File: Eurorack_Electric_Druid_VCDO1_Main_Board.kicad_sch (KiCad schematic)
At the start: 0 parts

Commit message: Multiboard work update
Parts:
- added C10, C11, C13, C14, C15, C9: 330pF, DIYSynthMNL:C_Rect_L7.0mm_W2.0mm_P5.00mm_BigPads, symbol Device:C
- added C12, C16: 150pF, DIYSynthMNL:C_Rect_L7.0mm_W2.0mm_P5.00mm_BigPads, symbol Device:C
- added C17, C18, C19, C24: 0.1uF, DIYSynthMNL:C_Rect_L7.0mm_W2.0mm_P5.00mm_BigPads, symbol Device:C
- added C19, C24: 22uF, DIYSynthMNL:CP_Radial_D4.0mm_P1.50mm, symbol Device:C_Polarized
- added C3, C4, C6, C7: 2.2uF, DIYSynthMNL:CP_Radial_D5.0mm_P2.50mm, symbol Device:C_Polarized
- added C5, C8: 100nF, DIYSynthMNL:C_Rect_L7.0mm_W2.0mm_P5.00mm_BigPads, symbol Device:C
- added D10, D11, D12, D13, D14, D15, D16, D3, D4, D5, D6, D7, D8, D9: BAT42, Diode_THT:D_DO-35_SOD27_P7.62mm_Horizontal, symbol Diode:BAT42
- added D13, D14: 4001, DIYSynthMNL:D_DO-41_SOD81_P7.62mm_Horizontal_BigPads, symbol Device:D
- added H3, H4: MountingHole_Pad, DIYSynthMNL:MountingHole_M3_Standoff_Pad, symbol Mechanical:MountingHole_Pad
- added J1: EuroPower_JST_3P, DIYSynthMNL:Eurorack_power_jst_3P, symbol DIYSynthMNL:JST_Eurorack_power_3P
- added J2: EURO_PWR_16P, DIYSynthMNL:IDC-Header_2x08_P2.54mm_Vertical, symbol DIYSynthMNL:EURO_PWR_16_PIN
- added Q1: 2N3904, Package_TO_SOT_THT:TO-92_Inline, symbol Transistor_BJT:2N3904
- added R1, R2: *10k, DIYSynthMNL:R_quarter_watt_L6.3mm_D2.5mm_P7.62mm, symbol Device:R
- added R10, R15, R18, R20, R25, R29, R33, R37, R47, R51, R9: 100K, DIYSynthMNL:R_quarter_watt_L6.3mm_D2.5mm_P7.62mm, symbol Device:R
- added R11, R19: 1K, DIYSynthMNL:R_quarter_watt_L6.3mm_D2.5mm_P7.62mm, symbol Device:R
- added R12, R16, R4, R5: 20K, DIYSynthMNL:R_quarter_watt_L6.3mm_D2.5mm_P7.62mm, symbol Device:R
- added R13, R17, R6, R7: 27K, DIYSynthMNL:R_quarter_watt_L6.3mm_D2.5mm_P7.62mm, symbol Device:R
- added R14, R8: 51K, DIYSynthMNL:R_quarter_watt_L6.3mm_D2.5mm_P7.62mm, symbol Device:R
- added R21: 1M, DIYSynthMNL:R_quarter_watt_L6.3mm_D2.5mm_P7.62mm, symbol Device:R
- added R22: 10K, DIYSynthMNL:R_quarter_watt_L6.3mm_D2.5mm_P7.62mm, symbol Device:R
- added R24, R27: 91K, DIYSynthMNL:R_quarter_watt_L6.3mm_D2.5mm_P7.62mm, symbol Device:R
- added R26, R31, R34, R38, R48, R52: 4K7, DIYSynthMNL:R_quarter_watt_L6.3mm_D2.5mm_P7.62mm, symbol Device:R
- added R28, R32, R35, R36, R39, R46, R49, R50, R53: 200K, DIYSynthMNL:R_quarter_watt_L6.3mm_D2.5mm_P7.62mm, symbol Device:R
- added R3: 10k, DIYSynthMNL:R_quarter_watt_L6.3mm_D2.5mm_P7.62mm, symbol Device:R
- added R30: 180K, DIYSynthMNL:R_quarter_watt_L6.3mm_D2.5mm_P7.62mm, symbol Device:R
- added RV1: 20K_V/Oct_Adjust, DIYSynthMNL:Potentiometer_Bourns_3296W_Vertical_BigPads, symbol Device:R_Potentiometer_Trim
- added RV2: 20K_Offset_trim, DIYSynthMNL:Potentiometer_Bourns_3296W_Vertical_BigPads, symbol Device:R_Potentiometer_Trim
- added RV4: 47K_Zero_Trim, DIYSynthMNL:Potentiometer_Bourns_3296W_Vertical_BigPads, symbol Device:R_Potentiometer_Trim
- added U1: 78M05, Package_TO_SOT_SMD:TO-252-2, symbol Regulator_Linear:LM78M05_TO252
- added U2: 79M05, Package_TO_SOT_SMD:TO-252-2, symbol Regulator_Linear:MC79M05_TO252
- added U3: VCDO1, DIYSynthMNL:DIP-18_W7.62mm_LongPads, symbol DIYSynthMNL:Druid_VCDO1_PIC16F1847
- added U4, U6: TL074, DIYSynthMNL:DIP-14_W7.62mm_LongPads, symbol Amplifier_Operational:TL074
- added U5, U7: TL072, DIYSynthMNL:DIP-8_W7.62mm_LongPads, symbol Amplifier_Operational:TL072
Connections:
- new net: R50.2, R51.1, R53.2, U7.6 (-)
- new net: R25.1, R27.2, RV1.2, RV1.3, U6.2 (-)
- new net: R25.2, R26.1, U6.1
- new net: R30.1, RV4.2, RV4.3
- new net: R28.2, R29.1, R30.2, U6.6 (-)
- new net: R29.2, R31.1, U6.7
- new net: C9.1, R4.2, R5.1
- new net: R14.2, R15.1, R18.2, U5.6 (-)
- new net: R15.2, R19.1, U5.7
- new net: R27.1, RV2.2, RV2.3
- new net: C16.2, R17.1, U4.12 (+)
- new net: R32.2, R33.1, R35.2, U6.9 (-)
- new net: R33.2, R34.1, U6.8
- new net: C14.2, R14.1, U4.13 (-), U4.14
- new net: R10.1, R8.2, R9.2, U5.2 (-)
- new net: R10.2, R11.1, U5.1
- new net: R51.2, R52.1, U7.7
- new net: C11.2, R5.2, U4.3 (+)
- new net: D3.2 (A), D4.1 (K), Q1.2 (B), R20.2, R21.1
- new net: C14.1, R13.2, R17.2
- new net: C10.2, R8.1, U4.6 (-), U4.7
- new net: R24.2, RV1.1
- new net: C13.1, R12.2, R16.1
- new net: R37.2, R38.1, U6.14
- new net: R3.2, U3.15 (Unused)
- new net: R36.2, R37.1, R39.2, U6.13 (-)
- new net: C9.2, R6.1, U4.1, U4.2 (-)
- new net: C13.2, R13.1, U4.8, U4.9 (-)
- new net: R46.2, R47.1, R49.2, U7.2 (-)
- new net: C15.2, R16.2, U4.10 (+)
- new net: C12.2, R7.1, U4.5 (+)
- new net: R47.2, R48.1, U7.1
- new net: C10.1, R6.2, R7.2
- new net +12V: C17.1, C18.1, C19.1, C19.1, C24.1, C3.1, D13.1 (K), U1.1 (VI), U4.4 (V+), U5.8 (V+), U6.4 (V+), U7.8 (V+)
- new net +12V_IN: D13.2 (A), J1.1 (+12v), J2.10 (+12V), J2.9 (+12V)
- new net +5V: C4.1, C5.1, D11.1 (K), D13.1 (K), D15.1 (K), D3.1 (K), D5.1 (K), D7.1 (K), D9.1 (K), R1.1, R22.1, R3.1, U1.3 (VO), U3.14 (+5V)
- new net -12V: C17.2, C18.2, C19.2, C24.2, C24.2, C6.2, D14.2 (A), U2.2 (VI), U4.11 (V-), U5.4 (V-), U6.11 (V-), U7.4 (V-)
- new net -12V_IN: D14.1 (K), J1.3 (-12v), J2.1 (-12V), J2.2 (-12V)
- new net -5V: C7.2, C8.2, R18.1, R2.2, R35.1, R39.1, R49.1, R53.1, R9.1, RV2.1, RV4.1, U2.3 (VO)
- new net AIN_Bitcrush_Control: D15.2 (A), D16.1 (K), R52.2, U3.9 (Bitcrush_Control)
- new net AIN_Freq_Mod_CV: D7.2 (A), D8.1 (K), R31.2, U3.11 (Freq_Mod_CV)
- new net AIN_Glide_Control: D13.2 (A), D14.1 (K), R48.2, U3.8 (Glide_Control)
- new net AIN_Note_CV: D5.2 (A), D6.1 (K), R26.2, U3.10 (Note_CV)
- new net AIN_Sub_Select_CV: D11.2 (A), D12.1 (K), R38.2, U3.18 (Sub_Select_CV)
- new net AIN_Waveform_CV: D10.1 (K), D9.2 (A), R34.2, U3.17 (Waveform_CV)
- new net Bitcrush_CV: R50.1
- new net DIN_Glide_Input: Q1.3 (C), R22.2, U3.13 (Glide_Input)
- new net DOUT_Main_Osc_Out: R4.1, U3.6 (Main_Osc_Out)
- new net DOUT_Sub_OSC_Out: R12.1, U3.16 (Sub_OSC_out)
- new net FM_CV: R28.1
- new net Freq_Course_Ctrl: U3.1 (Freq_Control)
- new net Freq_Fine_Ctrl: U3.2 (Fine_Control)
- new net GND: C11.1, C12.1, C15.1, C16.1, C19.2, C24.1, C3.2, C4.2, C5.2, C6.1, C7.1, C8.1, D10.2 (A), D12.2 (A), D14.2 (A), D16.2 (A), D4.2 (A), D6.2 (A), D8.2 (A), H3.1, H4.1, J1.2 (GND), J2.3 (GND), J2.4 (GND), J2.5 (GND), J2.6 (GND), J2.7 (GND), J2.8 (GND), Q1.1 (E), R1.2, R2.1, R21.2, U1.2 (GND), U2.1 (GND), U3.5 (0v), U5.3 (+), U5.5 (+), U6.10 (+), U6.12 (+), U6.3 (+), U6.5 (+), U7.3 (+), U7.5 (+)
- new net GlideTime_CV: R46.1
- new net Glide_OnOff_CV: R20.1
- new net MainOsc_Out: R11.2
- new net MainWaveSel_CV: R32.1
- new net MainWaveSel_Ctrl: U3.3 (Waveform_Control)
- new net Note_CV: R24.1
- new net SubOsc_Out: R19.2
- new net SubWaveSel_CV: R36.1
- new net SubWaveSel_Ctrl: U3.7 (Sub_Select_Control)
- no-connect marks 0 -> 8
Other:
- note added: "*Optional Load Resistor"
- note added: "0V-5V"
- note added: "18KHz Bessel Filter 24dB/Oct"
- note added: "Bitcrush CV"
- note added: "CV=Jacks Control=Pots"
- note added: "FM CV"
- note added: "Glide CV"
- note added: "Glide on/off CV"
- note added: "Main Wave Select CV"
- note added: "Main oscillator"
- note added: "Note CV"
- note added: "Output processing"
- note added: "Power"
- note added: "Sub Wave Select CV"
- note added: "Sub oscillator"
- note added: "The Druid datasheet has a design error with the negative 5 volt regulator."

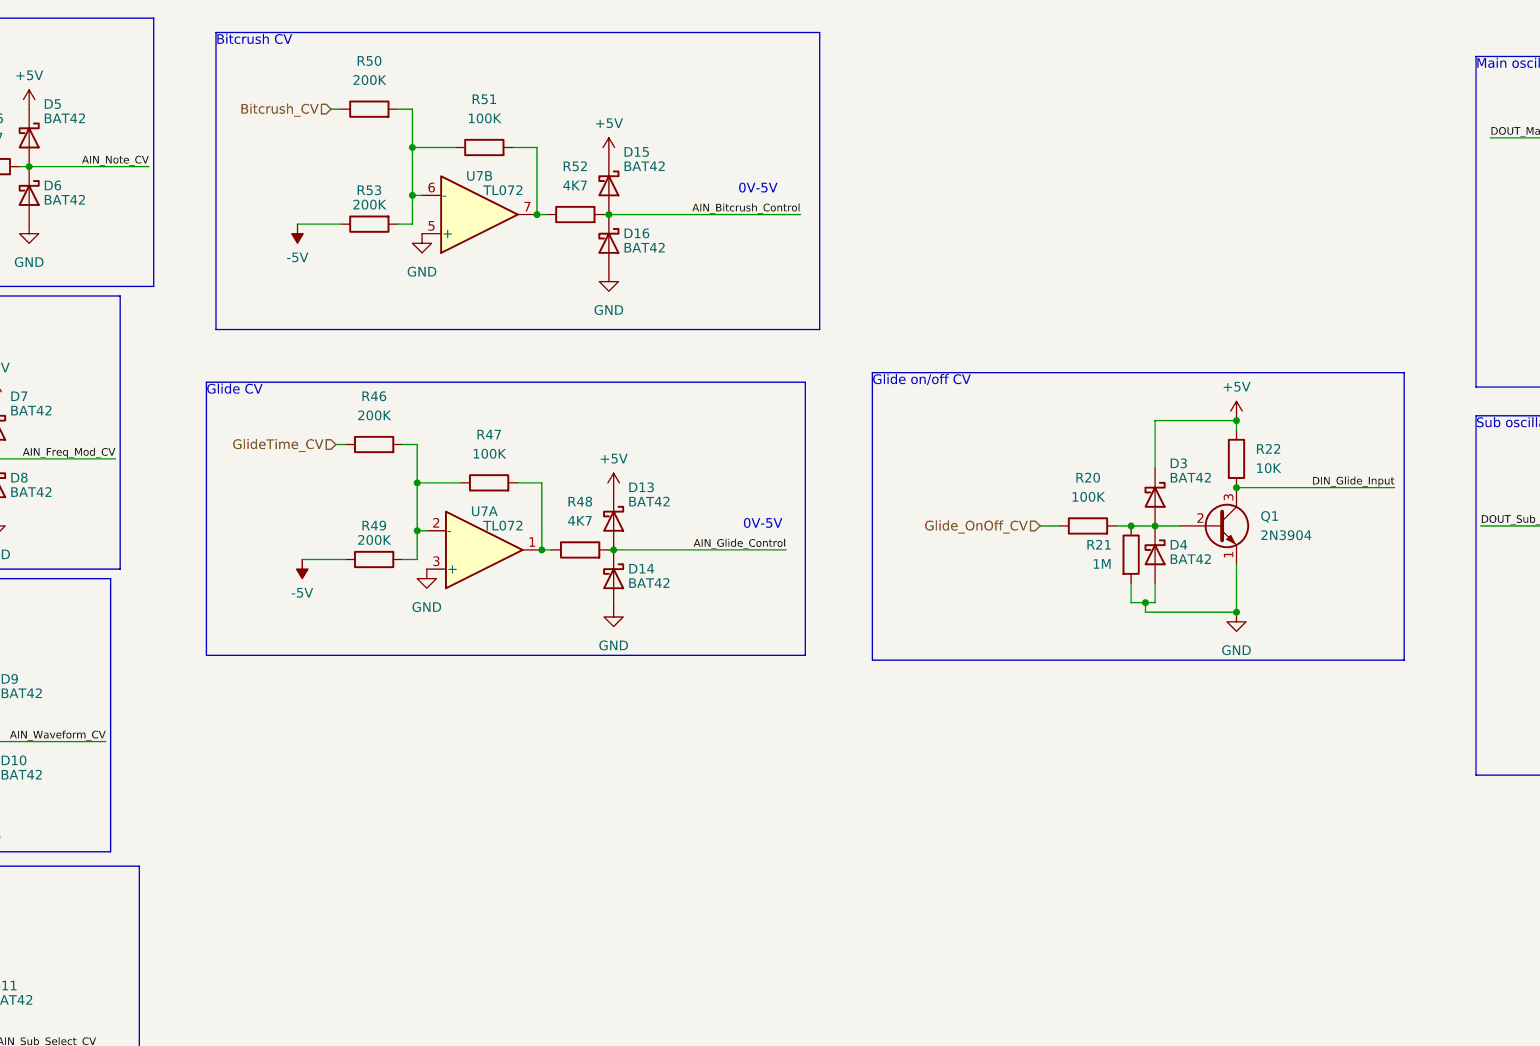
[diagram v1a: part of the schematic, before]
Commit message: updated schematic to rev 0.1.1
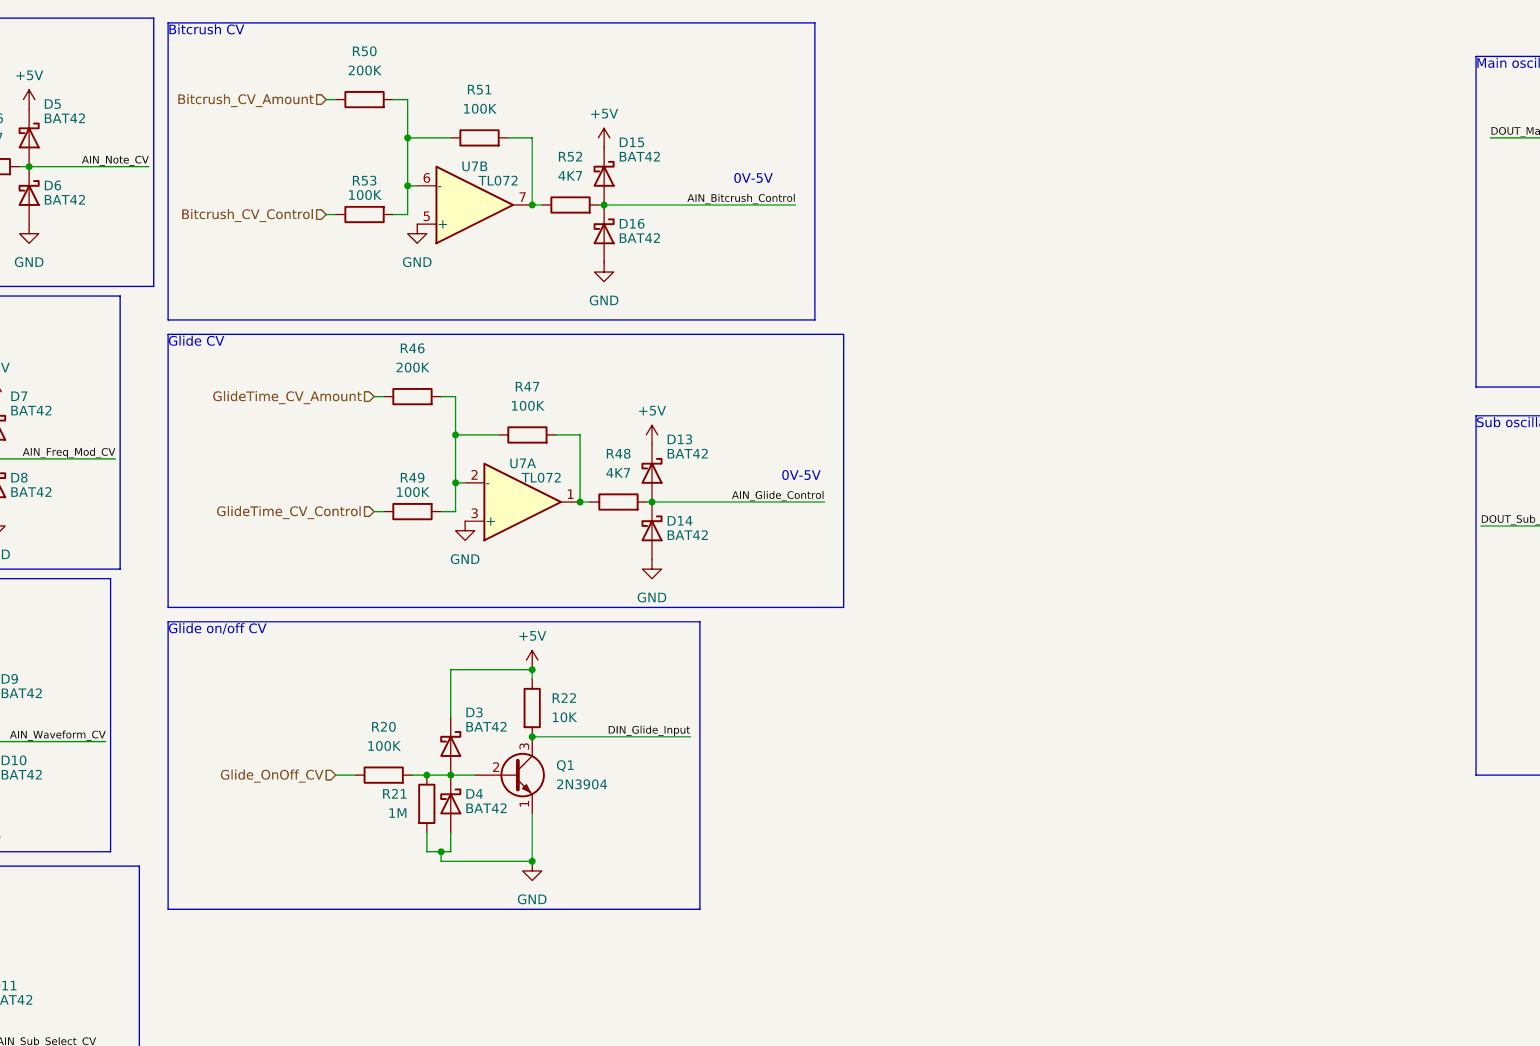
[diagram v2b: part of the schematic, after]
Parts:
- R49, R53: value 200K -> 100K
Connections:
- net -5V: no longer R49.1, R53.1
- net Bitcrush_CV renamed Bitcrush_CV_Amount
- net GlideTime_CV renamed GlideTime_CV_Amount
- new net Bitcrush_CV_Control: R53.1
- new net GlideTime_CV_Control: R49.1
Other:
- moved on the sheet: D13, D14, D15, D16, D3, D4, Q1, R20, R21, R22, R46, R47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

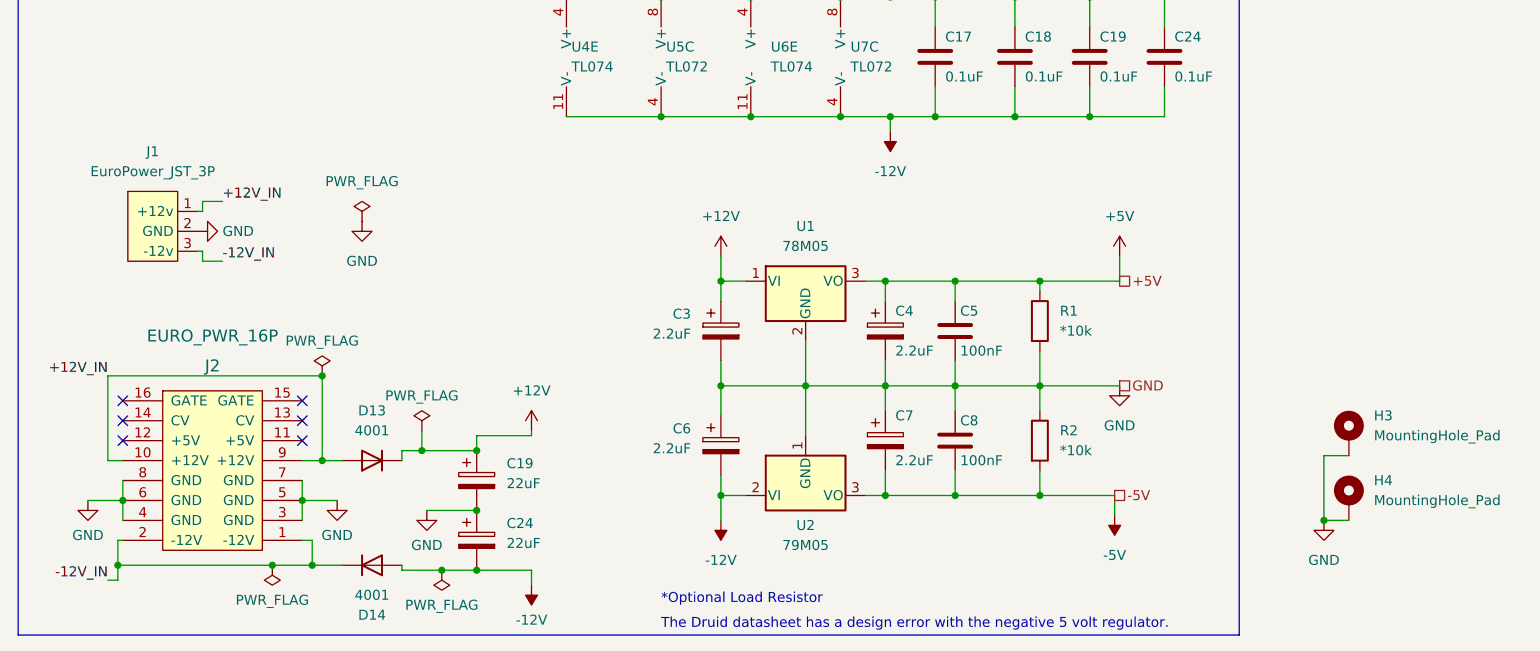
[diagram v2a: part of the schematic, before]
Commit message: updated to schematic revision 1.2
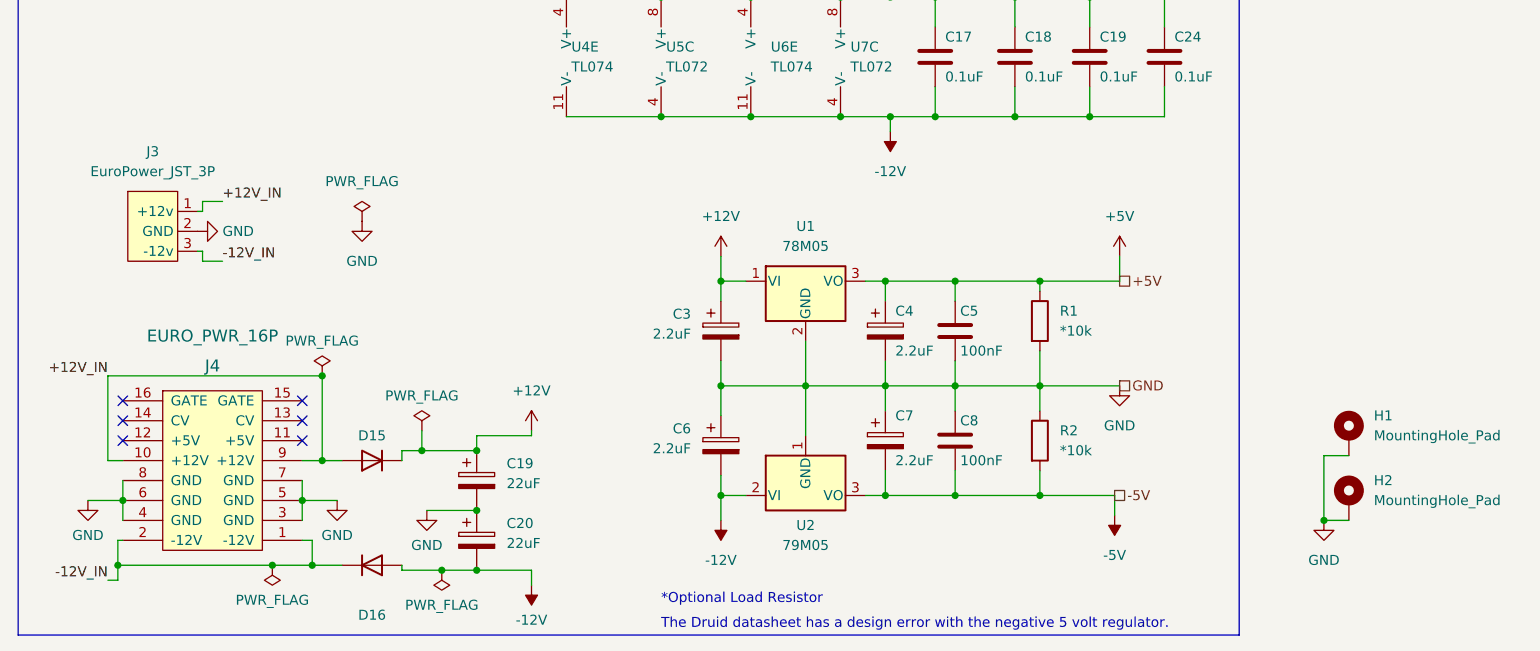
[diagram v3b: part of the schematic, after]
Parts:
- D15: renamed from D13; value 4001 -> ~
- D16: renamed from D14; value 4001 -> (none)
- renumbered C24 to C20, H3 to H1, H4 to H2, J1 to J3, J2 to J4
